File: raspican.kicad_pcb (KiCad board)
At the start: 2 copper layers, 85 x 56 mm, 22 parts, among them J1 CANBUS, J2 TTL_SERIAL, J3 TERMINATE, P1 CONN_13X2, U1 MCP2551-I/P, U4 MCP2515, Y1 16MHz

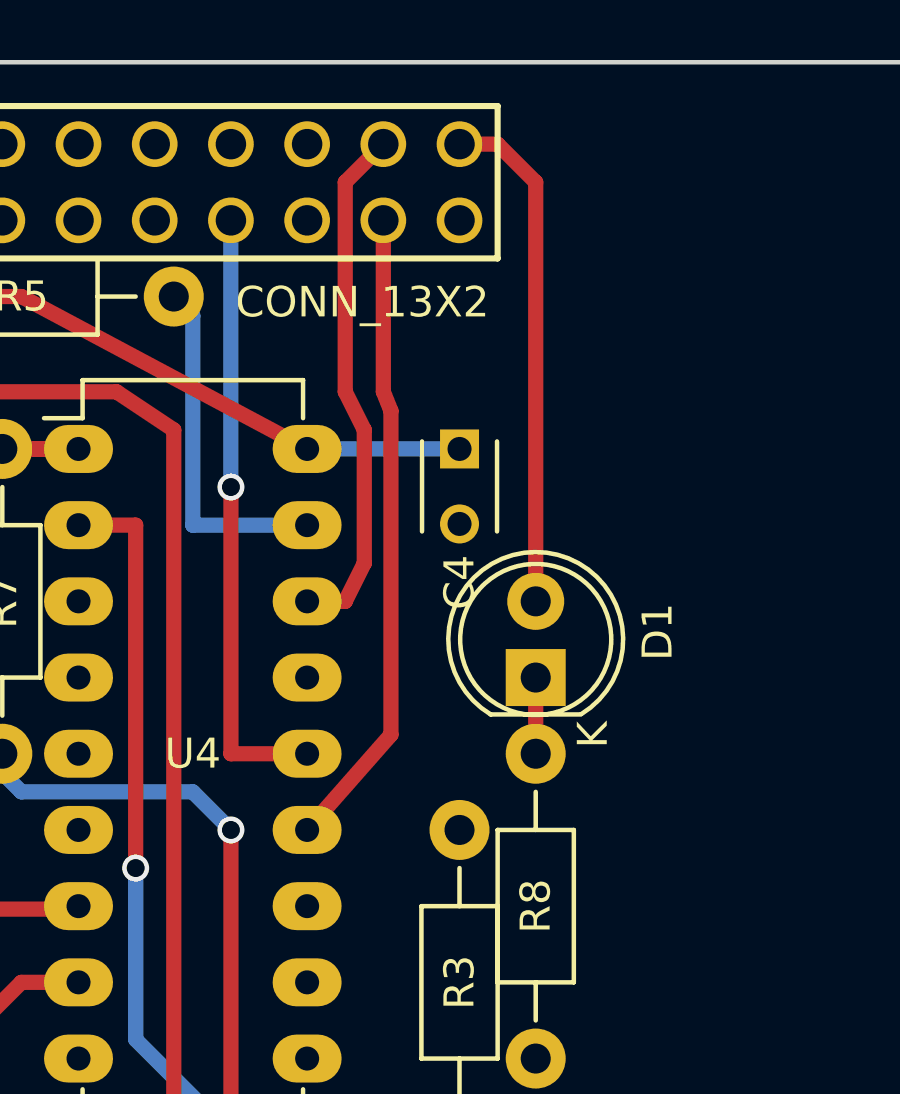
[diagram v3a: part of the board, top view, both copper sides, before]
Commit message: finish running traces on the board
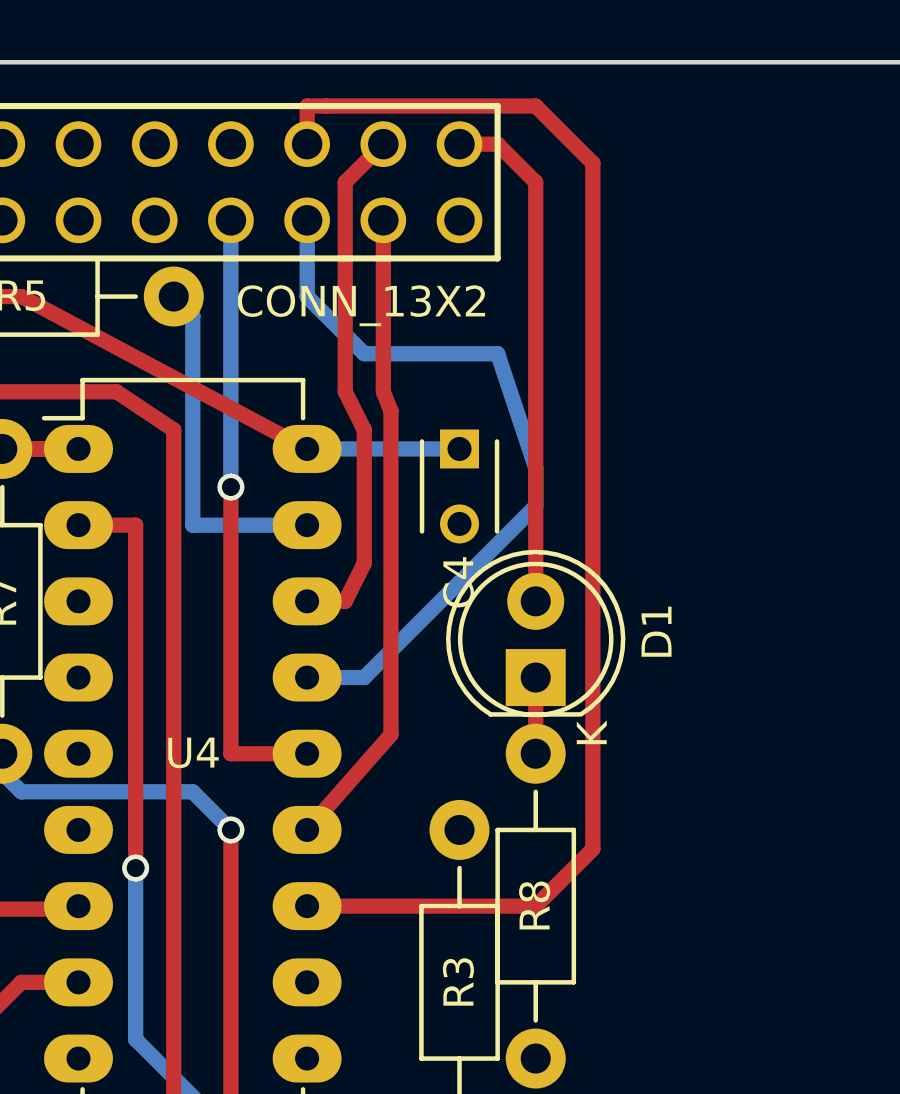
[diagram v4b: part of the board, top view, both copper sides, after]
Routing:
- net /GPIO25: track 0.00 -> 44.8 mm
- net /GPIO9(MISO): track 0.00 -> 25.0 mm
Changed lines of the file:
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@@
   (general
     (links 49)
-    (no_connects 17)
+    (no_connects 15)
     (area 127.666667 112.000001 242.904763 191.6478)
     (thickness 1.6)
     (drawings 41)
-    (tracks 106)
+    (tracks 120)
     (zones 0)
     (modules 22)
@@
   (segment (start 168.62 139.16) (end 168.62 148.05) (width 0.508) (layer F.Cu) (net 29))
   (via (at 168.62 139.16) (size 0.9) (drill 0.6) (layers F.Cu B.Cu) (net 29))
+  (segment (start 171.16 130.27) (end 171.16 132.81) (width 0.508) (layer B.Cu) (net 31) (status 400000))
+  (segment (start 173.065 145.51) (end 171.16 145.51) (width 0.508) (layer B.Cu) (net 31) (status 800000))
+  (segment (start 178.78 139.795) (end 173.065 145.51) (width 0.508) (layer B.Cu) (net 31))
+  (segment (start 178.78 138.525) (end 178.78 139.795) (width 0.508) (layer B.Cu) (net 31))
+  (segment (start 177.51 134.715) (end 178.78 138.525) (width 0.508) (layer B.Cu) (net 31))
+  (segment (start 173.065 134.715) (end 177.51 134.715) (width 0.508) (layer B.Cu) (net 31))
+  (segment (start 171.16 132.81) (end 173.065 134.715) (width 0.508) (layer B.Cu) (net 31))
+  (segment (start 171.16 127.73) (end 171.16 126.46) (width 0.508) (layer F.Cu) (net 32) (status 400000))
+  (segment (start 171.16 126.46) (end 171.795 126.46) (width 0.508) (layer F.Cu) (net 32))
+  (segment (start 171.795 126.46) (end 178.78 126.46) (width 0.508) (layer F.Cu) (net 32))
+  (segment (start 178.78 126.46) (end 180.685 128.365) (width 0.508) (layer F.Cu) (net 32))
+  (segment (start 180.685 128.365) (end 180.685 151.225) (width 0.508) (layer F.Cu) (net 32))
+  (segment (start 180.685 151.225) (end 178.78 153.13) (width 0.508) (layer F.Cu) (net 32))
+  (segment (start 178.78 153.13) (end 171.16 153.13) (width 0.508) (layer F.Cu) (net 32) (status 800000))
   (segment (start 173.7 130.27) (end 173.7 135.985) (width 0.508) (layer F.Cu) (net 33))
   (segment (start 173.954 147.415) (end 171.16 150.59) (width 0.508) (layer F.Cu) (net 33))
@@
   (segment (start 172.43 129) (end 172.43 135.985) (width 0.508) (layer F.Cu) (net 34))
   (segment (start 168.62 173.45) (end 171.16 173.45) (width 0.508) (layer B.Cu) (net 36))
-  (segment (start 173.7 164.56) (end 176.24 160.75) (width 0.508) (layer B.Cu) (net 36) (status 800000))
+  (segment (start 173.7 164.56) (end 176.24 160.75) (width 0.508) (layer B.Cu) (net 36))
   (segment (start 173.7 172.18) (end 173.7 164.56) (width 0.508) (layer B.Cu) (net 36))
   (segment (start 171.16 173.45) (end 173.7 172.18) (width 0.508) (layer B.Cu) (net 36))
@@
   (segment (start 163.54 137.89) (end 161 137.89) (width 0.508) (layer F.Cu) (net 38))
   (segment (start 161 137.89) (end 163.54 137.89) (width 0.508) (layer F.Cu) (net 38))
-  (segment (start 161 148.05) (end 161 148.685) (width 0.508) (layer B.Cu) (net 39) (status C00000))
-  (segment (start 161 148.685) (end 161.635 149.32) (width 0.508) (layer B.Cu) (net 39) (status 400000))
+  (segment (start 161 148.05) (end 161 148.685) (width 0.508) (layer B.Cu) (net 39))
+  (segment (start 161 148.685) (end 161.635 149.32) (width 0.508) (layer B.Cu) (net 39))
   (segment (start 161.635 149.32) (end 167.35 149.32) (width 0.508) (layer B.Cu) (net 39))
   (segment (start 167.35 149.32) (end 168.62 150.59) (width 0.508) (layer B.Cu) (net 39))
@@
   (segment (start 168.62 150.59) (end 168.62 160.75) (width 0.508) (layer F.Cu) (net 39))
   (segment (start 168.62 160.75) (end 173.7 165.83) (width 0.508) (layer F.Cu) (net 39))
-  (segment (start 173.7 165.83) (end 176.24 165.83) (width 0.508) (layer F.Cu) (net 39) (status 800000))
-  (segment (start 176.24 173.45) (end 175.605 173.45) (width 0.508) (layer F.Cu) (net 40) (status C00000))
-  (segment (start 175.605 173.45) (end 171.795 169.64) (width 0.508) (layer F.Cu) (net 40) (status 400000))
+  (segment (start 173.7 165.83) (end 176.24 165.83) (width 0.508) (layer F.Cu) (net 39))
+  (segment (start 176.24 173.45) (end 175.605 173.45) (width 0.508) (layer F.Cu) (net 40))
+  (segment (start 175.605 173.45) (end 171.795 169.64) (width 0.508) (layer F.Cu) (net 40))
   (segment (start 171.795 169.64) (end 171.795 169.005) (width 0.508) (layer F.Cu) (net 40))
   (via (at 171.795 169.005) (size 0.9) (drill 0.6) (layers F.Cu B.Cu) (net 40))
@@
   (via (at 165.445 151.86) (size 0.9) (drill 0.6) (layers F.Cu B.Cu) (net 40))
   (segment (start 165.445 151.86) (end 165.445 140.43) (width 0.508) (layer F.Cu) (net 40))
-  (segment (start 165.445 140.43) (end 163.54 140.43) (width 0.508) (layer F.Cu) (net 40) (status 800000))
+  (segment (start 165.445 140.43) (end 163.54 140.43) (width 0.508) (layer F.Cu) (net 40))
 )
